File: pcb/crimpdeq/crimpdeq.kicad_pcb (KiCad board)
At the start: 4 copper layers, 30 x 30 mm, 59 parts, among them J10 A-_Cable_Pad, J11 E+_Cable_Pad, J12 E-_Cable_Pad, J2 USB4105-GF-A, J5 B-_Cable_Pad, J6 SW+_Cable_Pad, J7 B+_Cable_Pad, J8 SW-_Cable_Pad, J9 A+_Cable_Pad, Q2 DMG3415U, U1 ESP32-C3-MINI-1, U2 MCP73831T-2ACI/OT, U3 ADS1220, U5 MAX17048G+T10, U6 SY8088

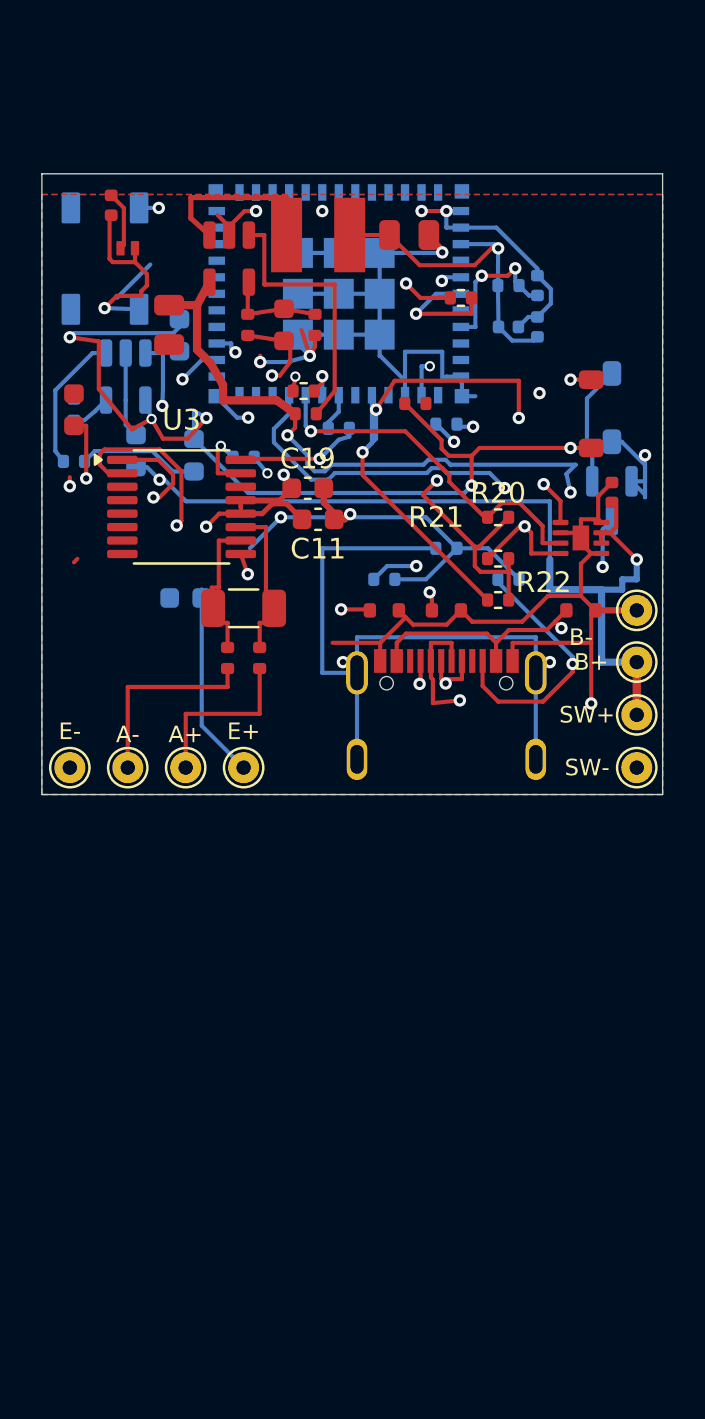
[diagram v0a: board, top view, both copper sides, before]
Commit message: Revert "Revision 3 (#26)"
This reverts commit 90a500b67033c502f14e333f57f99a449d93ac6c.
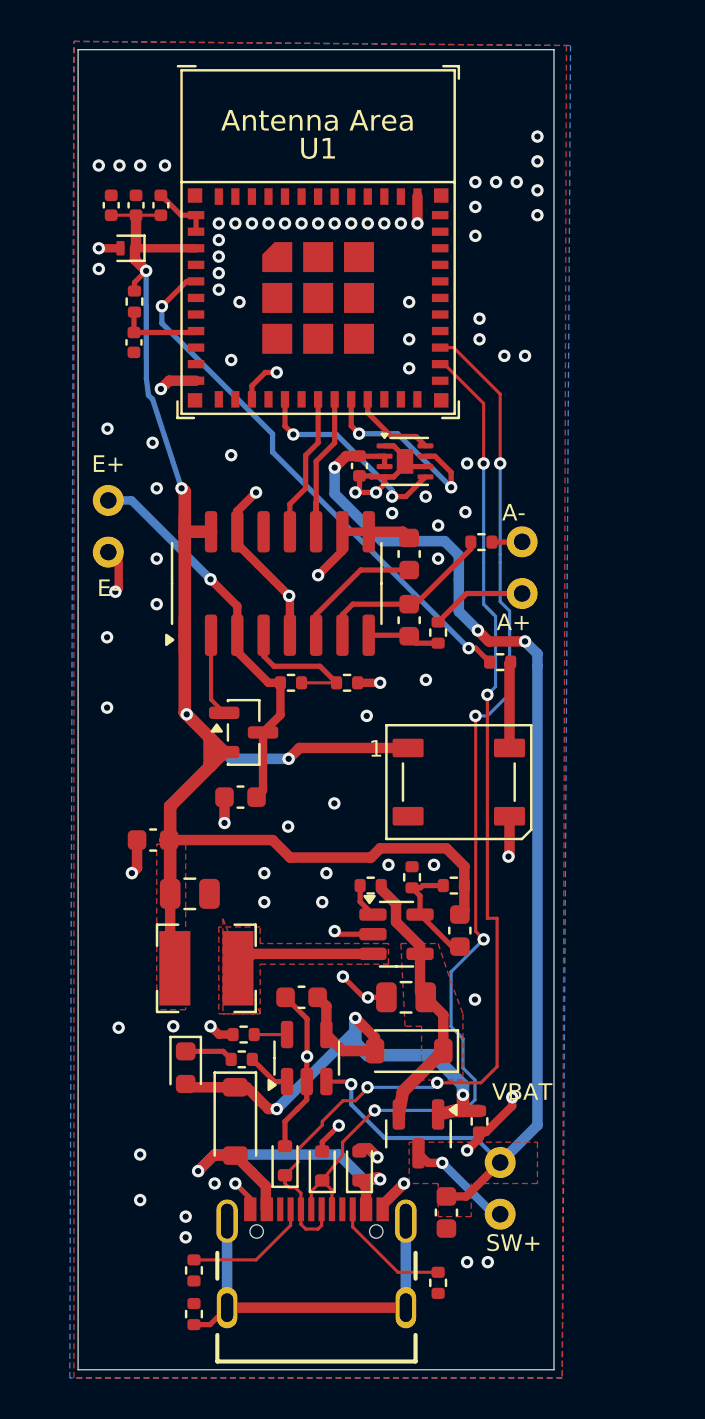
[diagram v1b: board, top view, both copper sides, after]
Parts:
- removed C19: 0.1uF, Capacitor_SMD:C_0603_1608Metric
- removed J10: A-_Cable_Pad, TestPoint:TestPoint_THTPad_D1.5mm_Drill0.7mm
- removed J11: E+_Cable_Pad, TestPoint:TestPoint_THTPad_D1.5mm_Drill0.7mm
- removed J12: E-_Cable_Pad, TestPoint:TestPoint_THTPad_D1.5mm_Drill0.7mm
- removed J5: B-_Cable_Pad, TestPoint:TestPoint_THTPad_D1.5mm_Drill0.7mm
- removed J6: SW+_Cable_Pad, TestPoint:TestPoint_THTPad_D1.5mm_Drill0.7mm
- removed J7: B+_Cable_Pad, TestPoint:TestPoint_THTPad_D1.5mm_Drill0.7mm
- removed J8: SW-_Cable_Pad, TestPoint:TestPoint_THTPad_D1.5mm_Drill0.7mm
- removed J9: A+_Cable_Pad, TestPoint:TestPoint_THTPad_D1.5mm_Drill0.7mm
- removed R20, R21, R22: 10kR 1%, Resistor_SMD:R_0402_1005Metric
- removed R23, R24, R25, R26: 47R 1%, Resistor_SMD:R_0402_1005Metric
- added J3: Loadcell_Pads, External_Cable_Pads_Left, F.Cu at (130.7, 69.4)
- added J4: Power_Sense_Pads, External_Cable_Pads_Right, F.Cu at (150.7, 78.2)
- added Q1: SS8550, Package_TO_SOT_SMD:SOT-23, F.Cu at (137.2, 79.4)
- added R5: 12kR 1%, Resistor_SMD:R_0402_1005Metric, F.Cu at (139.5, 77.0)
- added R6: 8k2R 1%, Resistor_SMD:R_0402_1005Metric, F.Cu at (142.2, 77.0)
- C1, C10, C2, C3, C5, C6, D1, D2, D4, R1, R13, R17, R18, R19, R2, R3: moved to F.Cu
- C12: footprint Capacitor_SMD:C_1206_3216Metric -> Capacitor_SMD:C_0603_1608Metric
- J2: footprint Crimpdeq:GCT_USB4105-GF-A -> Rust_Board:GCT_USB4105-GF-A
- Q2: footprint Crimpdeq:SOT-23 -> Package_TO_SOT_SMD:SOT-23; moved to F.Cu
- U1: footprint Crimpdeq:ESP32-C3-MINI-1 -> PCM_Espressif:ESP32-C3-MINI-1; moved to F.Cu
- U2: footprint Crimpdeq:MCP73831_SOT-23-5 -> Package_TO_SOT_SMD:SOT-23-5; moved to F.Cu
- U3: value ADS1220 -> HX711; footprint Package_SO:TSSOP-16_4.4x5mm_P0.65mm -> Package_SO:SOP-16_3.9x9.9mm_P1.27mm
- U6: footprint Crimpdeq:SY8088_SOT-23-5 -> Package_TO_SOT_SMD:SOT-23-5
- moved C6 39.7 mm to (147.0, 102.6), turned to -90 degrees
- moved R17 39.0 mm to (134.8, 107.5), turned to 90 degrees
- moved D8 38.3 mm to (136.8, 98.2), turned to -90 degrees
- moved L1 35.8 mm to (135.4, 90.8), turned to 180 degrees
- moved R9 34.8 mm to (148.6, 98.2), turned to -90 degrees
- moved R19 34.6 mm to (134.8, 105.4), turned to -90 degrees
- moved C15 34.5 mm to (145.1, 92.2), turned to 180 degrees
- moved R18 34.2 mm to (146.6, 106.0), turned to -90 degrees
- moved U2 34.1 mm to (140.2, 95.1), turned to 90 degrees
- moved U6 33.6 mm to (144.6, 89.2), turned to 0 degrees
- moved C17 33.6 mm to (134.6, 87.2)
- moved D2 32.6 mm to (145.2, 94.8), turned to 180 degrees
- moved C5 32.5 mm to (140.0, 92.2), turned to 0 degrees
- moved Q2 32.0 mm to (145.7, 98.8)
- moved R2 31.3 mm to (137.2, 94.0), turned to 0 degrees
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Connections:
- net Buck_Coil renamed /Buck_Coil
- net IO6_SCL renamed IO6_SDA
- net IO7_SDA renamed IO7_SCL
- C10 pad 1: +3V3 -> E+
- C11 pad 1: +3V3 -> GND
- C11 pad 2: GND -> Net-(U3-VBG)
- C12 pad 1: Net-(U3-AIN0) -> Net-(U3-INA+)
- C12 pad 2: Net-(U3-AIN1) -> Net-(U3-INA-)
- R7 pad 1: Net-(U3-AIN0) -> Net-(U3-INA+)
- R8 pad 1: Net-(U3-AIN1) -> Net-(U3-INA-)
- U1 pad 13: IO1_MISO -> unconnected-(U1-GPIO1/ADC1_CH1/XTAL_32K_N-Pad13)
- U1 pad 18: IO4_MOSI -> IO4_DATA
- U1 pad 37: GND -> (no net)
- U1 pad 38: GND -> (no net)
- U1 pad 39: GND -> (no net)
- U1 pad 40: GND -> (no net)
- U1 pad 41: GND -> (no net)
- U1 pad 42: GND -> (no net)
- U1 pad 43: GND -> (no net)
- U1 pad 44: GND -> (no net)
- U1 pad 45: GND -> (no net)
- U1 pad 46: GND -> (no net)
- U1 pad 47: GND -> (no net)
- U1 pad 48: GND -> (no net)
- U1 pad 49: GND -> (no net)
- U1 pad 50: GND -> (no net)
- U1 pad 51: GND -> (no net)
- U1 pad 52: GND -> (no net)
- U1 pad 53: GND -> (no net)
- U1 pad 6: IO3_CS -> unconnected-(U1-GPIO3/ADC1_CH3-Pad6)
- U3 pad 1: ADS_SCLK -> +3V3
- U3 pad 10: Net-(U3-AIN1) -> GND
- U3 pad 11: Net-(U3-AIN0) -> IO5_SCK
- U3 pad 12: +3V3 -> IO4_DATA
- U3 pad 13: +3V3 -> unconnected-(U3-XO-Pad13)
- U3 pad 14: unconnected-(U3-~{DRDY}-Pad14) -> GND
- U3 pad 15: ADS_DOUT -> +3V3
- U3 pad 16: ADS_DIN -> +3V3
- U3 pad 2: ADS_CS -> Net-(Q1-B)
- U3 pad 3: GND -> E+
- U3 pad 4: GND -> Net-(U3-VFB)
- U3 pad 6: unconnected-(U3-AIN3/REFN1-Pad6) -> Net-(U3-VBG)
- U3 pad 7: unconnected-(U3-AIN2-Pad7) -> Net-(U3-INA-)
- U3 pad 8: GND -> Net-(U3-INA+)
- U3 pad 9: +3V3 -> GND
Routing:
- net GND: track 137.2 -> 63.5 mm, vias 13 -> 98
- net +3V3: track 116.5 -> 78.2 mm, vias 8 -> 4
- net ADS_CS: track 35.8 -> 0.00 mm, vias 2 -> 0
- net Net-(D4-DIN): track 31.1 -> 4.17 mm, vias 2 -> 0
- net VSYS: track 39.9 -> 13.1 mm, vias 3 -> 0
- net VBUS: track 53.1 -> 28.3 mm, vias 5 -> 3
- net IO1_MISO: track 24.0 -> 0.00 mm, vias 2 -> 0
- net ADS_SCLK: track 21.1 -> 0.00 mm, vias 2 -> 0
- net IO10_ALRT: track 30.0 -> 10.1 mm, vias 4 -> 2
- net E+: track 0.00 -> 19.9 mm, vias 0 -> 1
- net IO7_SCL: track 22.7 -> 4.10 mm, vias 2 -> 0
- net Net-(J2-SHELL_GND-PadS1): track 35.0 -> 18.9 mm, vias 2 -> 0
- net IO2_LED: track 10.2 -> 26.1 mm
- net USB_D+: track 37.7 -> 53.3 mm, vias 3 -> 4
- net USB_D-: track 40.2 -> 54.1 mm, vias 3 -> 4
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- added copper zone on F.Cu, net +3V3
- added copper zone on F.Cu, net +BATT
- added copper zone on F.Cu, net /Buck_Coil
- added copper zone on F.Cu, net VSYS
- removed copper zone on In2.Cu, net +3V3
- removed copper zone on In1.Cu, net GND
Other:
- board size 30 x 30 mm -> 23 x 63.8 mm
- copper layers 4 -> 2
- board text removed: "A+"
- board text removed: "A-"
- board text removed: "B+"
- board text removed: "B-"
- board text removed: "E+"
- board text removed: "E-"
- board text removed: "SW+"
- board text removed: "SW-"

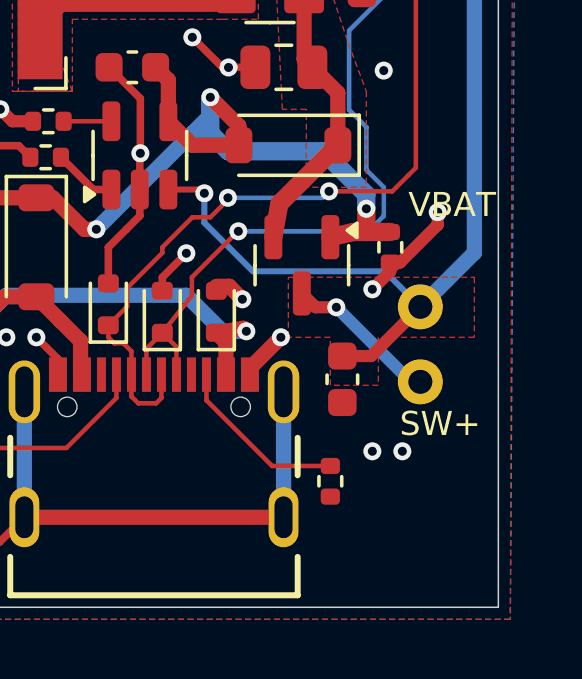
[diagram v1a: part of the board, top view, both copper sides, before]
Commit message: feat: add battery negative pad
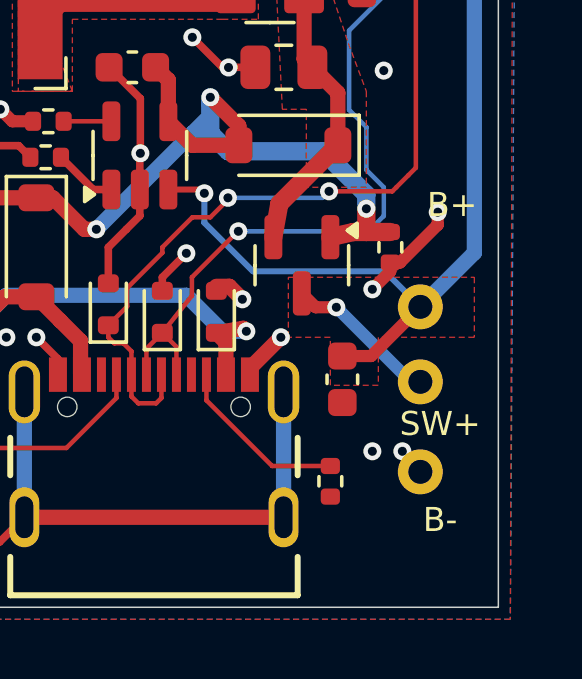
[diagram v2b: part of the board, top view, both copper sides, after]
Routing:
- net GND: track 63.5 -> 64.4 mm
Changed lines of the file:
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@@
 			)
 		)
-		(fp_text user "VBAT"
+		(fp_text user "B-"
+			(at -0.4 29.1 0)
+			(layer "F.SilkS")
+			(effects
+				(font
+					(size 0.8 0.8)
+					(thickness 0.12)
+				)
+			)
+		)
+		(fp_text user "B+"
 			(at 0 18.6 0)
 			(layer "F.SilkS")
@@
 			(pintype "passive")
 		)
+		(pad "5" thru_hole circle
+			(at -1.06 27.5)
+			(size 1.5 1.5)
+			(drill 0.8)
+			(layers "*.Cu" "*.Mask")
+			(remove_unused_layers no)
+			(net "GND")
+			(pinfunction "B-")
+			(pintype "passive")
+		)
 		(embedded_fonts no)
 	)
@@
 		(net "GND")
 	)
+	(segment
+		(start 149.6 105.685)
+		(end 149 105)
+		(width 0.4064)
+		(layer "B.Cu")
+		(net "GND")
+	)

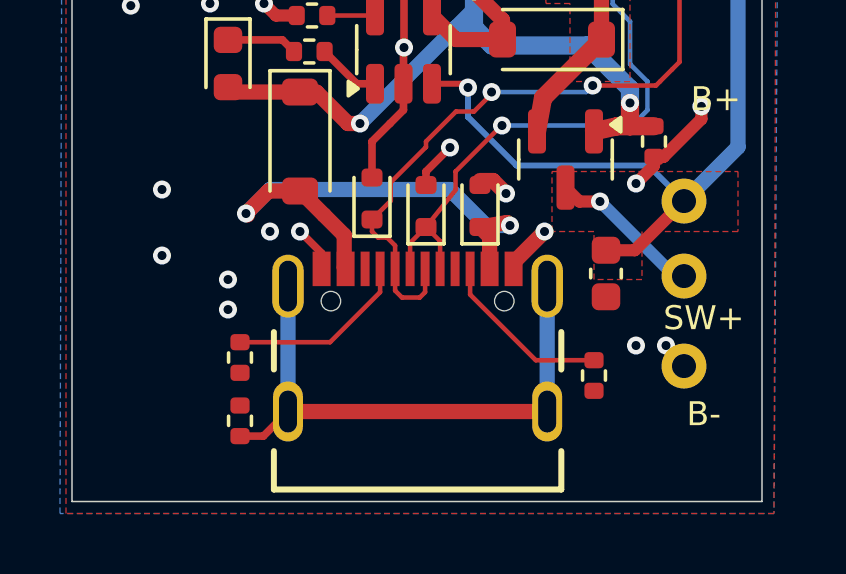
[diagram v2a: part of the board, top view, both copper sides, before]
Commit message: feat: align usb-c connector with board edge
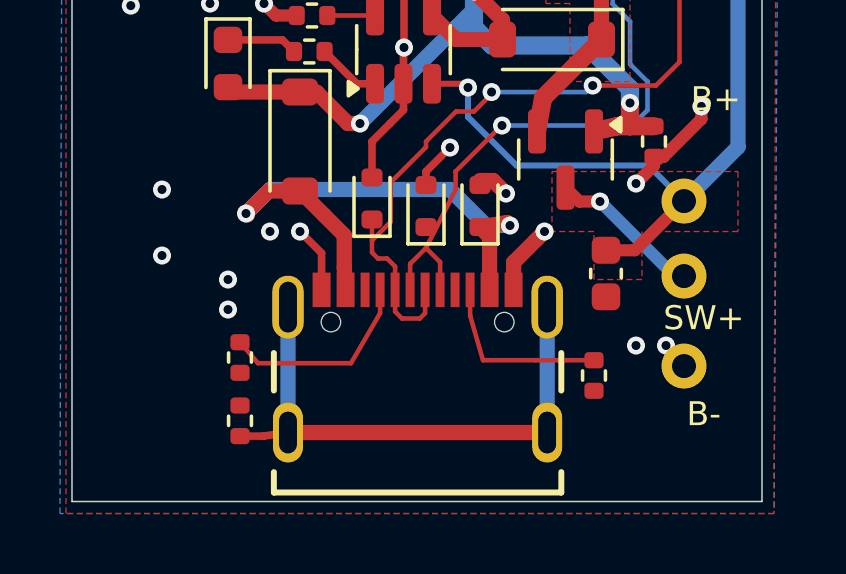
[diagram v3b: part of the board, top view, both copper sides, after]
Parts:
- moved J2 0.70 mm to (140.7, 107.9)
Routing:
- net GND: track 64.4 -> 65.8 mm
- net USB_D-: track 54.1 -> 55.5 mm
- net Net-(D8-A): track 17.6 -> 19.0 mm
- net USB_D+: track 53.3 -> 53.9 mm
- net Net-(J2-CC1): track 6.14 -> 6.73 mm
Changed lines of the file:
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@@
 	(footprint "Rust_Board:GCT_USB4105-GF-A"
 		(layer "F.Cu")
-		(at 140.72 107.2)
+		(at 140.72 107.9)
 		(property "Reference" "J2"
 			(at -1.825 -8.135 0)
@@
 		(fp_line
 			(start -4.79 1.32)
-			(end -4.79 2.6)
+			(end -4.79 2)
 			(stroke
 				(width 0.2)
@@
 		)
 		(fp_line
-			(start -4.79 2.6)
-			(end 4.79 2.6)
+			(start -4.79 2)
+			(end 4.79 2)
 			(stroke
 				(width 0.2)
@@
 		)
 		(fp_line
-			(start 4.79 2.6)
+			(start 4.79 2)
 			(end 4.79 1.32)
 			(stroke
@@
 	)
 	(segment
-		(start 141 101.05)
+		(start 141 101.75)
 		(end 141.98513 99.81487)
 		(width 0.1524)
@@
 	)
 	(segment
-		(start 140.47 102.445)
-		(end 140.47 101.58)
+		(start 140.47 103.145)
+		(end 140.47 102.28)
 		(width 0.1524)
 		(layer "F.Cu")
@@
 	)
 	(segment
-		(start 141.47 101.52)
-		(end 141 101.05)
+		(start 141.47 102.22)
+		(end 141 101.75)
 		(width 0.1524)
 		(layer "F.Cu")
@@
 	)
 	(segment
-		(start 140.47 101.58)
-		(end 141 101.05)
+		(start 140.47 102.28)
+		(end 141 101.75)
 		(width 0.1524)
 		(layer "F.Cu")
@@
 	)
 	(segment
-		(start 141.47 102.445)
-		(end 141.47 101.52)
+		(start 141.47 103.145)
+		(end 141.47 102.22)
 		(width 0.1524)
 		(layer "F.Cu")
@@
 	)
 	(segment
-		(start 143.92 102.445)
+		(start 143.92 103.145)
 		(end 143.92 102.230485)
 		(width 0.508)
@@
 	)
 	(segment
-		(start 137.52 102.445)
+		(start 137.52 103.145)
 		(end 137.52 101.92)
 		(width 0.254)
@@
 	)
 	(segment
-		(start 138.32 102.445)
+		(start 138.32 103.145)
 		(end 138.274 102.399)
 		(width 0.508)
@@
 	(segment
 		(start 143.12 101.37)
-		(end 143.12 102.445)
+		(end 143.12 103.145)
 		(width 0.508)
 		(layer "F.Cu")
@@
 	)
 	(segment
-		(start 139.97 103.17)
-		(end 139.97 102.445)
+		(start 139.97 103.87)
+		(end 139.97 103.145)
 		(width 0.1524)
 		(layer "F.Cu")
@@
 	)
 	(segment
-		(start 139.2 100.8)
-		(end 139.8262 100.1738)
+		(start 139.2 101.5)
+		(end 139.8262 100.8738)
 		(width 0.1524)
 		(layer "F.Cu")
@@
 	)
 	(segment
-		(start 140.7924 103.4)
-		(end 140.2 103.4)
+		(start 140.7924 104.1)
+		(end 140.2 104.1)
 		(width 0.1524)
 		(layer "F.Cu")
@@
 	)
 	(segment
-		(start 139.2 101.2)
+		(start 139.2 101.9)
 		(end 139.2 100.8)
 		(width 0.1524)
@@
 	)
 	(segment
-		(start 139.7024 101.4)
-		(end 139.4 101.4)
+		(start 139.7024 102.1)
+		(end 139.4 102.1)
 		(width 0.1524)
 		(layer "F.Cu")
@@
 	)
 	(segment
-		(start 139.4 101.4)
-		(end 139.2 101.2)
+		(start 139.4 102.1)
+		(end 139.2 101.9)
 		(width 0.1524)
 		(layer "F.Cu")
@@
 	)
 	(segment
-		(start 139.97 102.445)
-		(end 139.97 101.6676)
+		(start 139.97 103.145)
+		(end 139.97 102.3676)
 		(width 0.1524)
 		(layer "F.Cu")
@@
 	)
 	(segment
-		(start 140.97 102.445)
-		(end 140.97 103.2224)
+		(start 140.97 103.145)
+		(end 140.97 103.9224)
 		(width 0.1524)
 		(layer "F.Cu")
@@
 	)
 	(segment
-		(start 139.97 101.6676)
-		(end 139.7024 101.4)
+		(start 139.97 102.3676)
+		(end 139.7024 102.1)
 		(width 0.1524)
 		(layer "F.Cu")
@@
 	)
 	(segment
-		(start 140.2 103.4)
-		(end 139.97 103.17)
+		(start 140.2 104.1)
+		(end 139.97 103.87)
 		(width 0.1524)
 		(layer "F.Cu")
@@
 	)
 	(segment
-		(start 139.8262 100.1738)
+		(start 139.8262 100.8738)
 		(end 139.8262 99.55893)
 		(width 0.1524)
@@
 	)
 	(segment
-		(start 140.97 103.2224)
-		(end 140.7924 103.4)
+		(start 140.97 103.9224)
+		(end 140.7924 104.1)
 		(width 0.1524)
 		(layer "F.Cu")
@@
 	)
 	(segment
-		(start 139.47 103.2224)
-		(end 139.47 102.445)
+		(start 139.47 103.9224)
+		(end 139.47 103.145)
+		(width 0.1524)
+		(layer "F.Cu")
+		(net "Net-(J2-CC1)")
+	)
+	(segment
+		(start 138.5 105.59)
+		(end 139.47 103.9224)
 		(width 0.1524)
 		(layer "F.Cu")
@@
 	(segment
 		(start 134.8 104.89)
-		(end 137.8024 104.89)
+		(end 135.4 105.59)
 		(width 0.1524)
 		(layer "F.Cu")
@@
 	)
 	(segment
-		(start 137.8024 104.89)
-		(end 139.47 103.2224)
+		(start 135.4 105.59)
+		(end 138.5 105.59)
 		(width 0.1524)
 		(layer "F.Cu")
@@
 	(segment
 		(start 144.659064 105.49)
-		(end 142.47 103.300936)
+		(end 142.9 105.49)
+		(width 0.1524)
+		(layer "F.Cu")
+		(net "Net-(J2-CC2)")
+	)
+	(segment
+		(start 142.47 104.000936)
+		(end 142.47 103.145)
 		(width 0.1524)
 		(layer "F.Cu")
@@
 	)
 	(segment
-		(start 142.47 103.300936)
-		(end 142.47 102.445)
+		(start 142.9 105.49)
+		(end 142.47 104.000936)
 		(width 0.1524)
 		(layer "F.Cu")
@@
 	(segment
 		(start 135.58 108.02)
-		(end 136.4 107.2)
+		(end 136.4 107.9)
 		(width 0.254)
 		(layer "F.Cu")
@@
 	)
 	(segment
-		(start 145.04 107.2)
-		(end 136.4 107.2)
+		(start 145.04 107.9)
+		(end 136.4 107.9)
 		(width 0.508)
 		(layer "F.Cu")
@@
 	)
 	(segment
-		(start 136.4 103.02)
-		(end 136.4 107.2)
+		(start 136.4 103.72)
+		(end 136.4 107.9)
 		(width 0.508)
 		(layer "B.Cu")
@@
 	)
 	(segment
-		(start 145.04 103.02)
-		(end 145.04 107.2)
+		(start 145.04 103.72)
+		(end 145.04 107.9)
 		(width 0.508)
 		(layer "B.Cu")

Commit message: feat: separate external pad groups
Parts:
- added J5: Battery_Switch_Pads, External_Battery_Switch_Pads_Left, F.Cu at (150.6, 101.6)
- J4: value Power_Sense_Pads -> Sense_Pads; footprint External_Cable_Pads_Right -> External_Sense_Pads_Right
- moved R13 24.6 mm to (133.4, 57.5), turned to -90 degrees
- moved J4 20.2 mm to (130.7, 81.3)
- moved R8 16.3 mm to (133.0, 74.6), turned to 90 degrees
- moved R7 14.3 mm to (132.5, 77.2), turned to 180 degrees
- moved C9 10.7 mm to (143.0, 81.2), turned to -90 degrees
- moved C17 8.33 mm to (140.6, 81.4), turned to -90 degrees
- moved C10 5.38 mm to (140.9, 78.8), turned to 0 degrees
- moved C12 3.40 mm to (143.4, 76.9), turned to 180 degrees
- moved R6 2.62 mm to (139.6, 76.7)
- moved R5 2.05 mm to (137.5, 76.7)
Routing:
- net Net-(D4-DIN): track 4.17 -> 30.0 mm, vias 0 -> 2
- net IO2_LED: track 26.1 -> 1.77 mm, vias 2 -> 0
- net +3V3: track 78.2 -> 65.0 mm, vias 4 -> 0
- net Net-(U3-INA+): track 3.80 -> 15.9 mm, vias 0 -> 2
- net Net-(U3-INA-): track 8.85 -> 14.6 mm, vias 0 -> 2
- net GND: track 65.8 -> 62.7 mm, vias 98 -> 101
- net Net-(U3-VFB): track 6.75 -> 3.77 mm
- net A+: track 4.63 -> 2.02 mm
- net E+: track 19.9 -> 17.9 mm
- net SW_BATT: track 5.17 -> 6.82 mm
- net A-: track 1.47 -> 2.62 mm
- net USB_D+: track 53.9 -> 52.8 mm, vias 4 -> 2
- net USB_D-: track 55.5 -> 54.7 mm
- net +BATT: track 58.9 -> 59.7 mm, vias 4 -> 3
